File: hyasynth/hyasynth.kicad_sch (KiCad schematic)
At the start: 38 parts, among them J1 Conn_01x04_Male, J2 Conn_01x02_Male, J3 Conn_01x06_Male, J4 Conn_01x02_Male, J5 Conn_01x04_Male, J6 AudioJack3_SwitchTR, SW1 Power Switch, SW10 G# Ab, SW11 A, SW12 A# Bb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

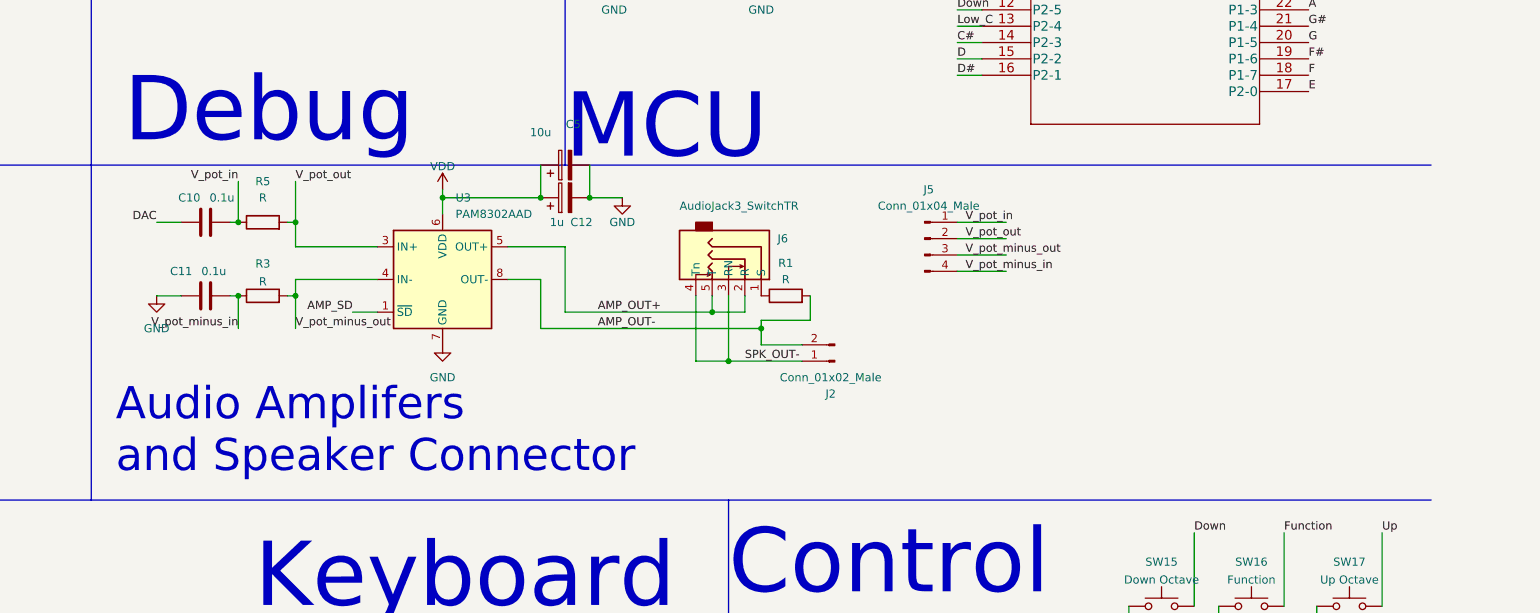
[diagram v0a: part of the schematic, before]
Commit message: Schematic changes
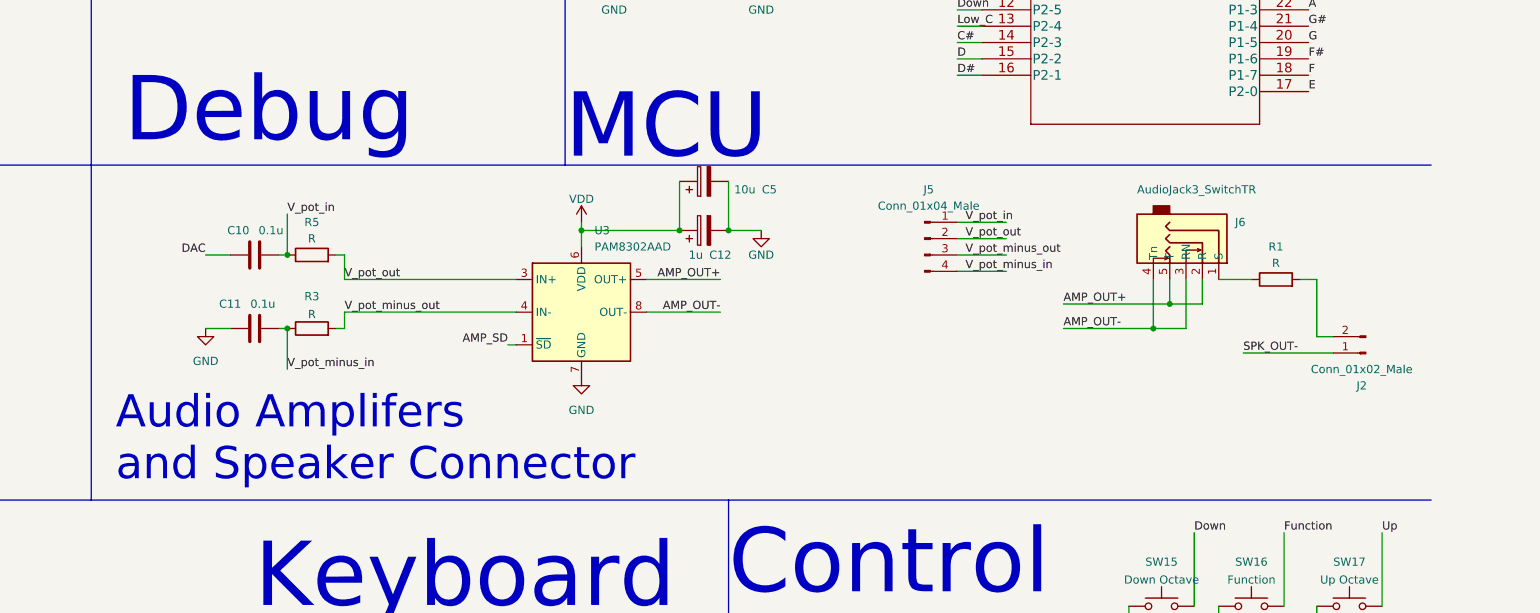
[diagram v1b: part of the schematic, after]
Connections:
- net AMP_OUT-: now also J6.3 (RN), J6.4 (Tn); no longer J2.2 (Pin_2), R1.2
- net SPK_OUT-: no longer J6.3 (RN), J6.4 (Tn)
- new net: J2.2 (Pin_2), R1.2
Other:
- moved on the sheet: C10, C11, C12, C5, J2, J6, R1, R3, R5, U3

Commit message: Schematic
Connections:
- net AMP_OUT-: now also J2.2 (Pin_2), R1.2; no longer J6.3 (RN), J6.4 (Tn)
- net SPK_OUT-: now also J6.3 (RN), J6.4 (Tn)
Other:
- note added: "Audio Amplifers"
- note added: "Speaker Conn. and Headphone Jack"
- note removed: "Audio Amplifers and Speaker Connector"
- moved on the sheet: C12, C5, J5, U3

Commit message: New Switch and Silkscreen changes
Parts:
- SW1: footprint Switch:Slide Switch -> powerSwitch:SK12D07VG4NSPA
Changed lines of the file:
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@@
     (property "Reference" "SW1" (id 0) (at 46.99 24.13 90))
     (property "Value" "Power Switch" (id 1) (at 52.07 26.67 90))
-    (property "Footprint" "Switch:Slide Switch" (id 2) (at 41.91 26.67 0)
+    (property "Footprint" "powerSwitch:SK12D07VG4NSPA" (id 2) (at 41.91 26.67 0)
       (effects (font (size 1.27 1.27)) hide)
     )
@@
     )
     (path "/8edc3100-86dd-4549-b6e6-d3e637e4160d"
-      (reference "SW1") (unit 1) (value "Power Switch") (footprint "Switch:Slide Switch")
+      (reference "SW1") (unit 1) (value "Power Switch") (footprint "powerSwitch:SK12D07VG4NSPA")
     )
     (path "/7e72304a-4161-4a22-8d65-75ee76dcdf69"

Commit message: Fab 2
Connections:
- net GPIO_1: now also J3.2 (Pin_2), U1.32 (P0-1); no longer J3.4 (Pin_4), U1.30 (P0-3)
- net GPIO_3: now also J3.4 (Pin_4), U1.30 (P0-3); no longer J3.2 (Pin_2), U1.32 (P0-1)
- net GPIO_4 renamed GPIO_0
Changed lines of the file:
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@@
     (effects (font (size 1.27 1.27)) (justify left bottom))
   )
-  (label "GPIO_4" (at 212.09 31.75 0)
+  (label "GPIO_0" (at 212.09 31.75 0)
     (effects (font (size 1.27 1.27)) (justify left bottom))
   )
@@
     (effects (font (size 1.27 1.27)) (justify left bottom))
   )
-  (label "GPIO_3" (at 266.7 34.29 0)
+  (label "GPIO_1" (at 266.7 34.29 0)
     (effects (font (size 1.27 1.27)) (justify left bottom))
   )
@@
     (effects (font (size 1.27 1.27)) (justify left bottom))
   )
-  (label "GPIO_4" (at 31.75 93.98 0)
+  (label "GPIO_0" (at 31.75 93.98 0)
     (effects (font (size 1.27 1.27)) (justify left bottom))
   )
@@
     (effects (font (size 1.27 1.27)) (justify left bottom))
   )
-  (label "GPIO_3" (at 31.75 96.52 0)
+  (label "GPIO_1" (at 31.75 96.52 0)
     (effects (font (size 1.27 1.27)) (justify left bottom))
   )
@@
     (effects (font (size 1.27 1.27)) (justify left bottom))
   )
-  (label "GPIO_1" (at 31.75 101.6 0)
+  (label "GPIO_3" (at 31.75 101.6 0)
     (effects (font (size 1.27 1.27)) (justify left bottom))
   )
@@
     (effects (font (size 1.27 1.27)) (justify left bottom))
   )
-  (label "GPIO_1" (at 266.7 39.37 0)
+  (label "GPIO_3" (at 266.7 39.37 0)
     (effects (font (size 1.27 1.27)) (justify left bottom))
   )
